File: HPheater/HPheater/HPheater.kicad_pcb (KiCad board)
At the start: 2 copper layers, 100 x 125 mm, 7 parts, among them J1 Conn_01x02_Male

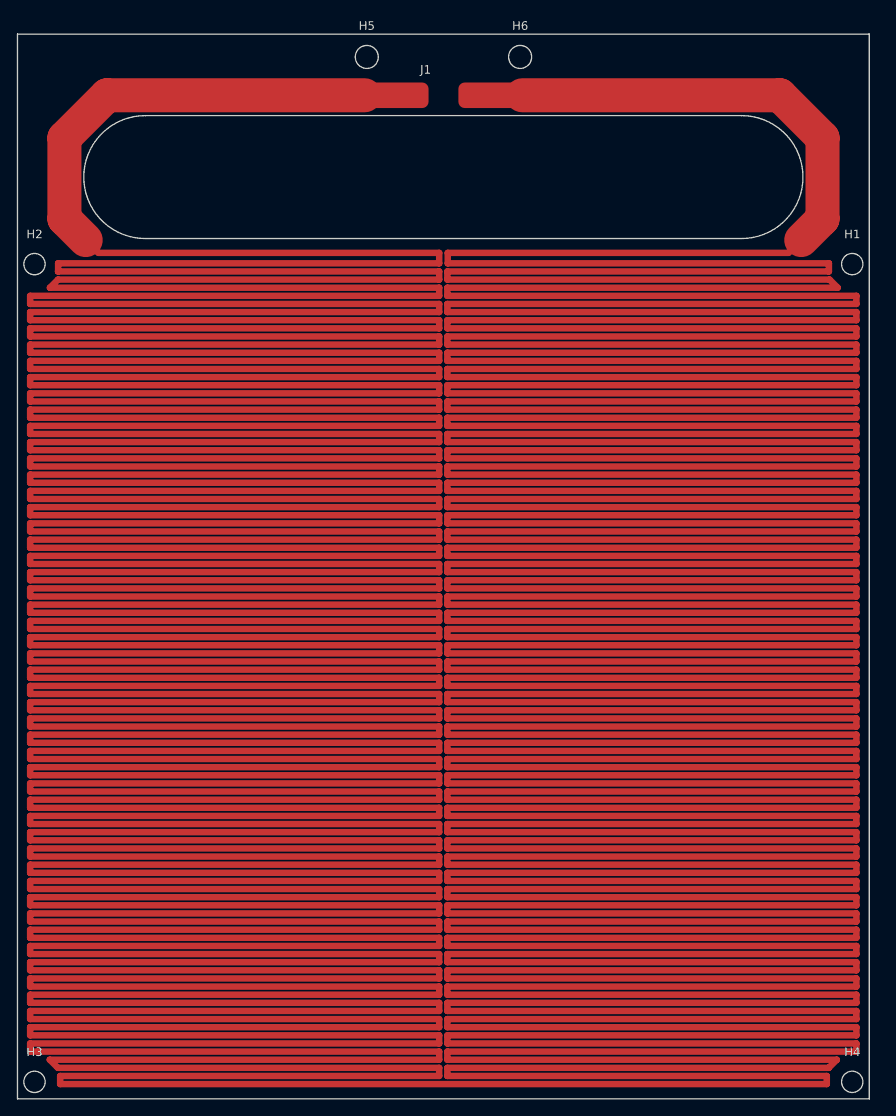
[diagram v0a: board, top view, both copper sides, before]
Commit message: released rev c - op amp swap not fixed!
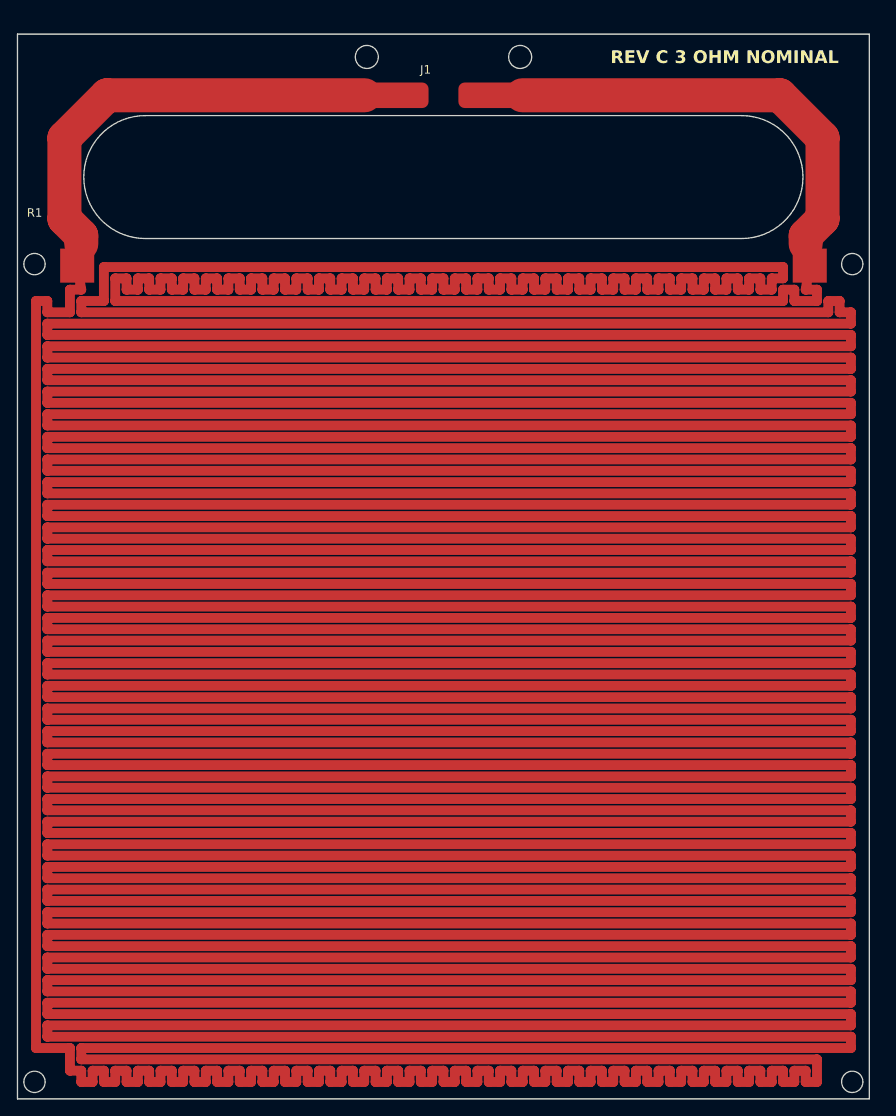
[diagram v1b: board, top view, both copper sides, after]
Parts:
- added R1: R, HPfootprint:Heater_3ohm, F.Cu at (172.0, 110.0)
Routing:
- net Net-(J1-Pin_1): track 5201.2 -> 50.6 mm
- net Net-(J1-Pin_2): track 4929.1 -> 50.6 mm
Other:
- board text added: "REV C 3 OHM NOMINAL"
